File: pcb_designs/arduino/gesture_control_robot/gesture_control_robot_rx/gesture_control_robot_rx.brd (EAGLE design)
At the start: 74.9 x 63.5 mm, 24 parts, among them IC1 ATMEGA328, IC2 7805, IC3 L293D, Q1 16MHZ

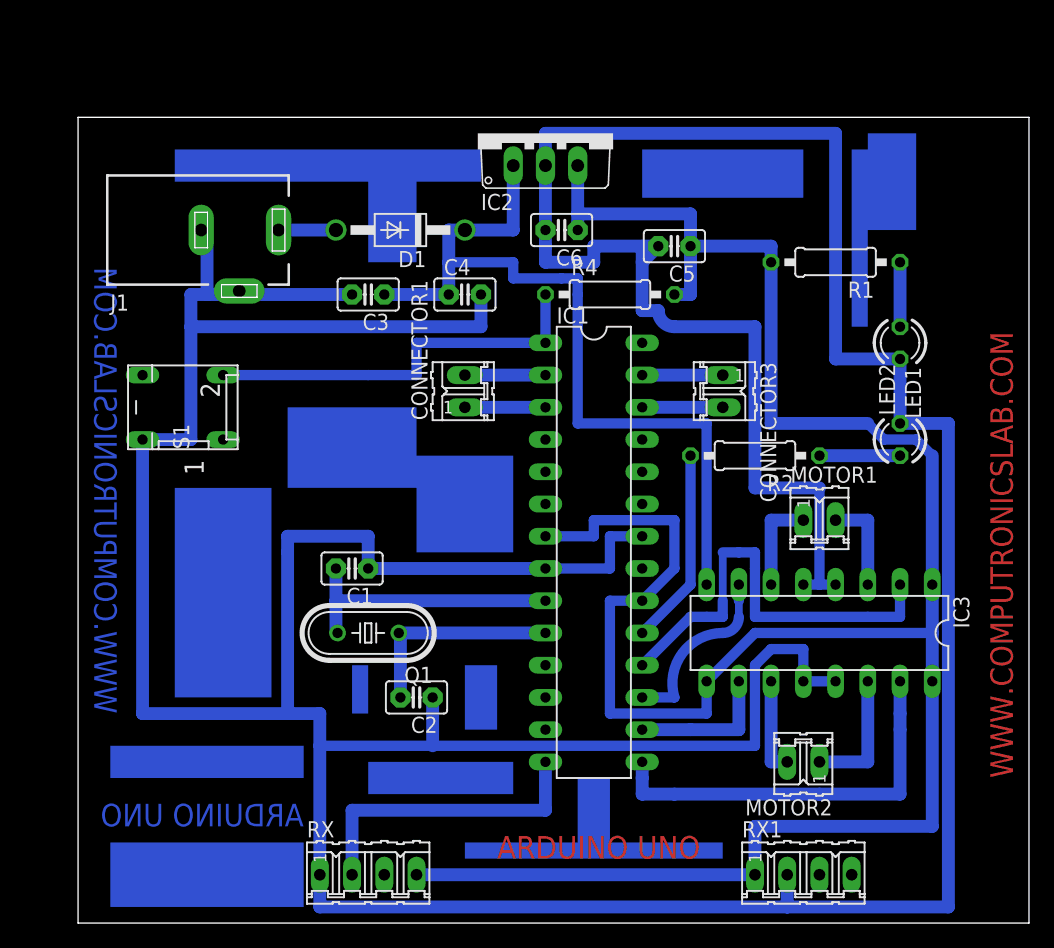
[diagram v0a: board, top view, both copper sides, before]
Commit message: add on off switch
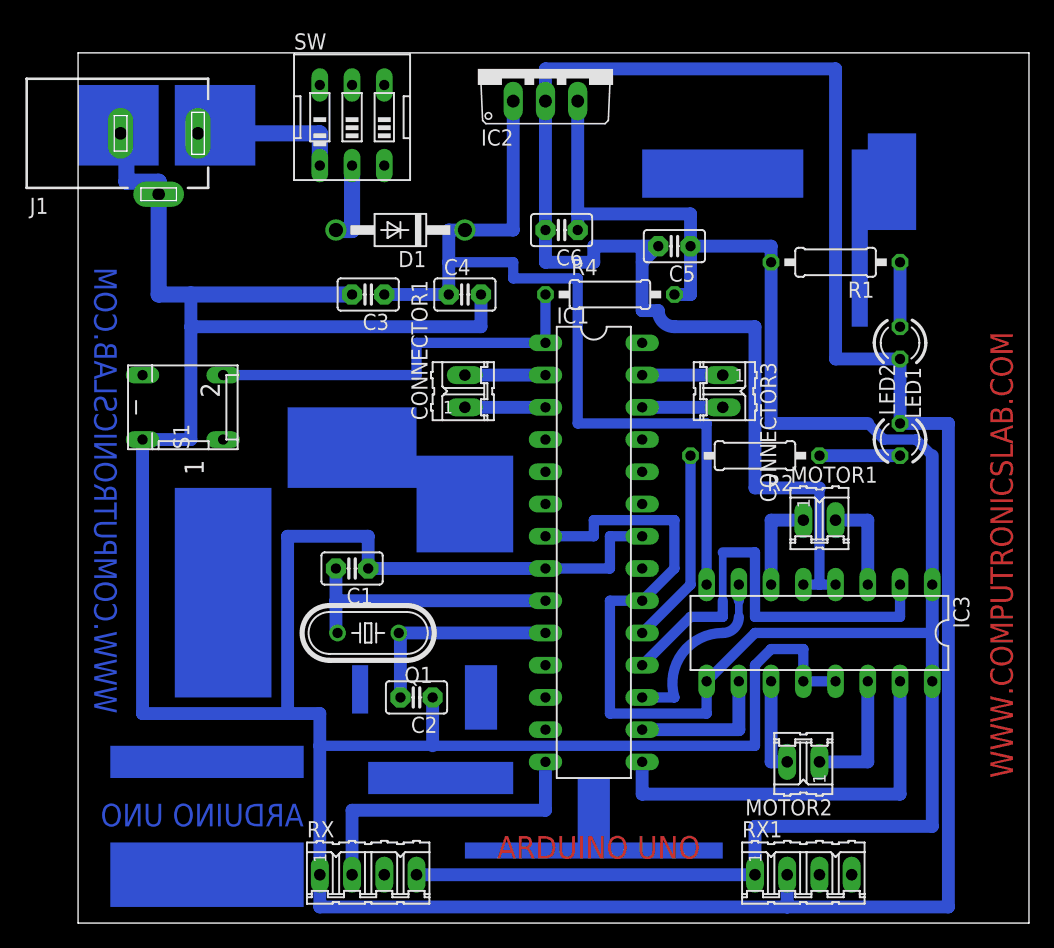
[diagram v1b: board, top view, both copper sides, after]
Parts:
- added SW: on/of button, special:EDG-03
- moved J1 9.92 mm to (19.1, 77.5)
- moved IC2 5.08 mm to (49.5, 82.5)
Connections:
- new net N$17: D1.A, SW.2
- net N$3: now also SW.1; no longer D1.A
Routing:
- net N$5: track 421.4 -> 444.0 mm
- net N$3: track 4.52 -> 12.1 mm
- net N$17: track 0.00 -> 6.35 mm
- net N$4: track 66.0 -> 71.1 mm
- net N$33: track 191.6 -> 196.7 mm
- net N$21: track 14.0 -> 12.7 mm
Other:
- board size 74.9 x 63.5 mm -> 74.9 x 68.6 mm
